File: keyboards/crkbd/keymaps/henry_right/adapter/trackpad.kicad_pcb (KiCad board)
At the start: 2 copper layers, 39.6 x 19.7 mm, 17 parts, among them J1 J1, U1 Elite-C-nf, U2 ProMicro, U3 U3, U4 NCP1117-2.85_SOT223

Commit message: 수정중
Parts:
- removed REF**: Hirose_FH12-12S-0.5SH_1x12-1MP_P0.50mm_Horizontal, Connector_FFC-FPC:Hirose_FH12-12S-0.5SH_1x12-1MP_P0.50mm_Horizontal
- removed REF**: SOIC-14_3.9x8.7mm_P1.27mm, Package_SO:SOIC-14_3.9x8.7mm_P1.27mm
- C1, C2: footprint Capacitor_Tantalum_SMD:CP_EIA-6032-15_Kemet-U -> Capacitor_SMD:C_0805_2012Metric
- C3: value 100pF -> 100nF
- J1: value J1 -> Conn_01x12; footprint trackpad:67997-410HLF -> Connector_FFC-FPC:Hirose_FH12-12S-0.5SH_1x12-1MP_P0.50mm_Horizontal
- U1: value Elite-C-nf -> Elite-C
- U3: value U3 -> NCP1117-3.3_SOT223; footprint trackpad:TXB0106PWR -> Package_TO_SOT_SMD:SOT-223-3_TabPin2
- U4: value NCP1117-2.85_SOT223 -> TXB0104D; footprint Package_TO_SOT_SMD:SOT-223-3_TabPin2 -> Package_SO:SOIC-14_3.9x8.7mm_P1.27mm
- moved J1 42.9 mm to (98.5, 63.0)
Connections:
- C2 pad 1: +2V8 -> +3V3
- C3 pad 1: +5V -> +3V3
- J1 pad 1: +2V8 -> +3V3
- J1 pad 10: GND -> TP_CS_3V3
- J1 pad 2: TP_SHUTDOWN_2V85 -> GND
- J1 pad 3: MOSI_2V85 -> Net-(J1-Pad3)
- J1 pad 4: SCK_2V85 -> Net-(J1-Pad4)
- J1 pad 5: GND -> Net-(J1-Pad5)
- J1 pad 6: TP_MOTION_2V85 -> Net-(J1-Pad6)
- J1 pad 7: TP_CS_2V85 -> Net-(J1-Pad7)
- J1 pad 8: MISO_2V85 -> MOSI_3V3
- J1 pad 9: Net-(J1-Pad9) -> PB6
- R1 pad 1: Net-(R1-Pad1) -> LVL_SHIFT
- U1 pad 1: TP_MOTION -> PD3
- U1 pad 25: PB7 -> LVL_SHIFT
- U1 pad 26: PD5 -> MAP_B0D5
- U1 pad 27: LVL_SHIFT -> MAP_B1C7
- U1 pad 28: TP_RESET -> MAP_B3F1
- U1 pad 29: TP_SHUTDOWN -> MAP_B2F0
- U2 pad 1: PB5 -> PD3
- U2 pad 12: Net-(U2-Pad12) -> PB5
- U2 pad 14: Net-(U2-Pad14) -> MAP_B2F0
- U2 pad 15: PD5 -> MAP_B3F1
- U2 pad 16: PB7 -> MAP_B1C7
- U2 pad 24: Net-(U2-Pad24) -> MAP_B0D5
- U3 pad 1: TP_MOTION_2V85 -> GND
- U3 pad 2: +2V8 -> +3V3
- U3 pad 3: TP_CS_2V85 -> +5V
- U4 pad 1: GND -> +3V3
- U4 pad 2: +2V8 -> TP_CS_3V3
- U4 pad 3: +5V -> MOSI_3V3
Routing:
- net TP_MOTION: track 28.5 -> 0.00 mm, vias 1 -> 0
- net PD3: track 0.00 -> 28.5 mm, vias 0 -> 1
- net +3V3: track 0.00 -> 21.2 mm
- net +2V8: track 48.1 -> 27.6 mm
- net TP_SHUTDOWN_2V85: track 11.0 -> 0.00 mm
- net +5V: track 24.3 -> 13.8 mm
- net MOSI_2V85: track 10.2 -> 0.00 mm
- net PB7: track 21.5 -> 16.1 mm
- net PD5: track 20.9 -> 17.4 mm
- net TP_RESET: track 4.20 -> 0.97 mm
- net PB5: track 34.8 -> 31.7 mm
- net TP_CS: track 32.9 -> 29.8 mm
- net TP_SHUTDOWN: track 15.3 -> 13.0 mm
- net LVL_SHIFT: track 2.09 -> 0.18 mm
- net TP_MOTION_2V85: track 15.7 -> 14.1 mm
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
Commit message: 배치 시작
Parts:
- removed C5: 100pF, Capacitor_SMD:C_0805_2012Metric
- removed C6: 100nF, Capacitor_SMD:C_0805_2012Metric
- removed R2, R4: 2.5K, Resistor_SMD:R_0805_2012Metric
- removed R3: 3.3K, Resistor_SMD:R_0805_2012Metric
- J1: moved to B.Cu
- moved C3 25.2 mm to (130.8, 66.0)
- moved J1 25.2 mm to (86.4, 85.1), turned to 90 degrees
- moved U4 22.7 mm to (84.9, 63.5)
- moved U3 22.0 mm to (104.8, 63.5)
- moved C4 21.7 mm to (124.5, 63.2)
- moved C1 21.1 mm to (119.0, 67.3)
- moved C2 14.6 mm to (115.9, 62.2)
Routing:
- net GND: track 61.5 -> 1.80 mm, vias 3 -> 0
- net PB5: track 31.7 -> 0.76 mm, vias 2 -> 0
- net TP_CS: track 29.8 -> 1.14 mm, vias 1 -> 0
- net PD3: track 28.5 -> 0.00 mm, vias 1 -> 0
- net +2V8: track 27.6 -> 0.00 mm
- net +3V3: track 21.2 -> 0.00 mm
- net PD5: track 17.4 -> 0.00 mm, vias 4 -> 0
- net PB7: track 16.1 -> 0.00 mm, vias 4 -> 0
- net SCK_2V85: track 14.9 -> 0.00 mm, vias 1 -> 0
- net TP_CS_2V85: track 14.9 -> 0.00 mm, vias 1 -> 0
- net MISO_2V85: track 14.7 -> 0.00 mm, vias 1 -> 0
- net TP_MOTION_2V85: track 14.1 -> 0.00 mm, vias 1 -> 0
- net TP_SHUTDOWN: track 13.0 -> 0.00 mm
- net MOSI: track 13.3 -> 0.80 mm
- net +5V: track 13.8 -> 2.82 mm
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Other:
- board text added: "GlidePoint Circle Adapter Henry Jian"
- board text removed: "Trackpad controller v1.1 Designed by vlukash"

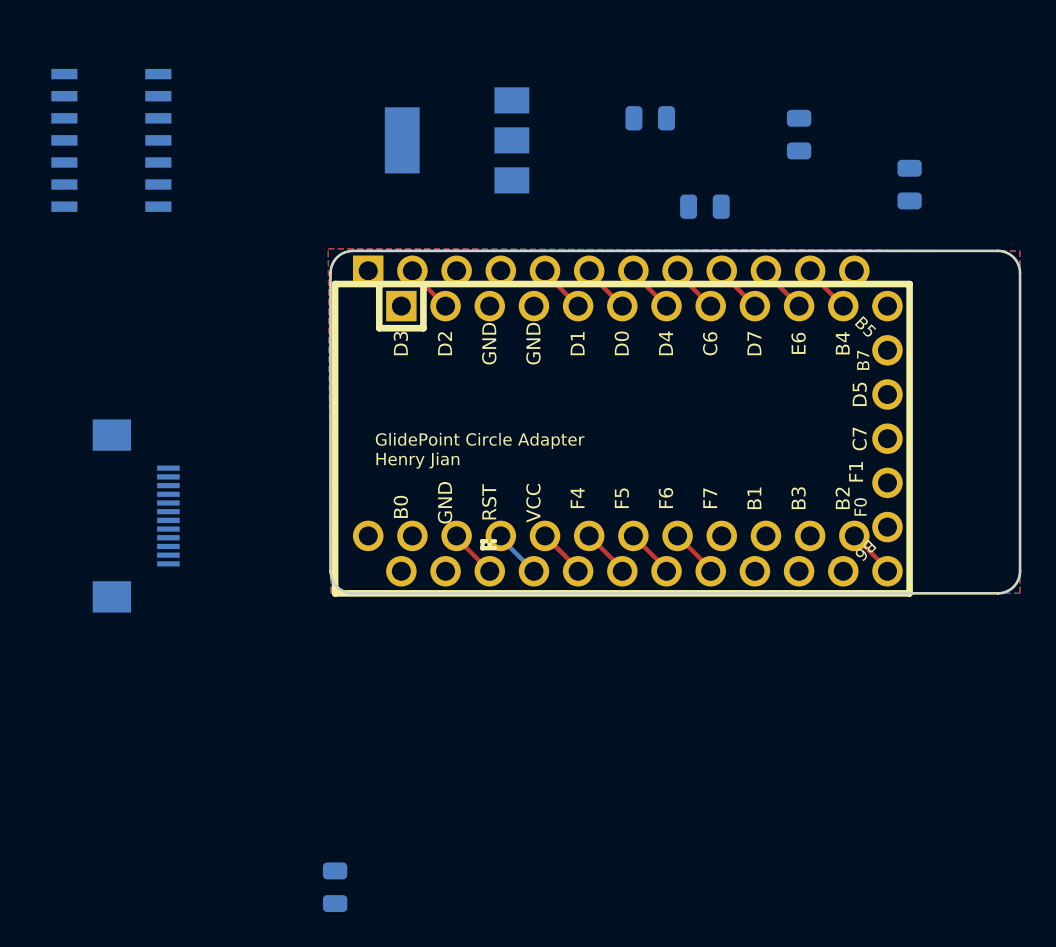
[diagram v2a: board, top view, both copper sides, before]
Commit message: 배치 거의 끝난듯
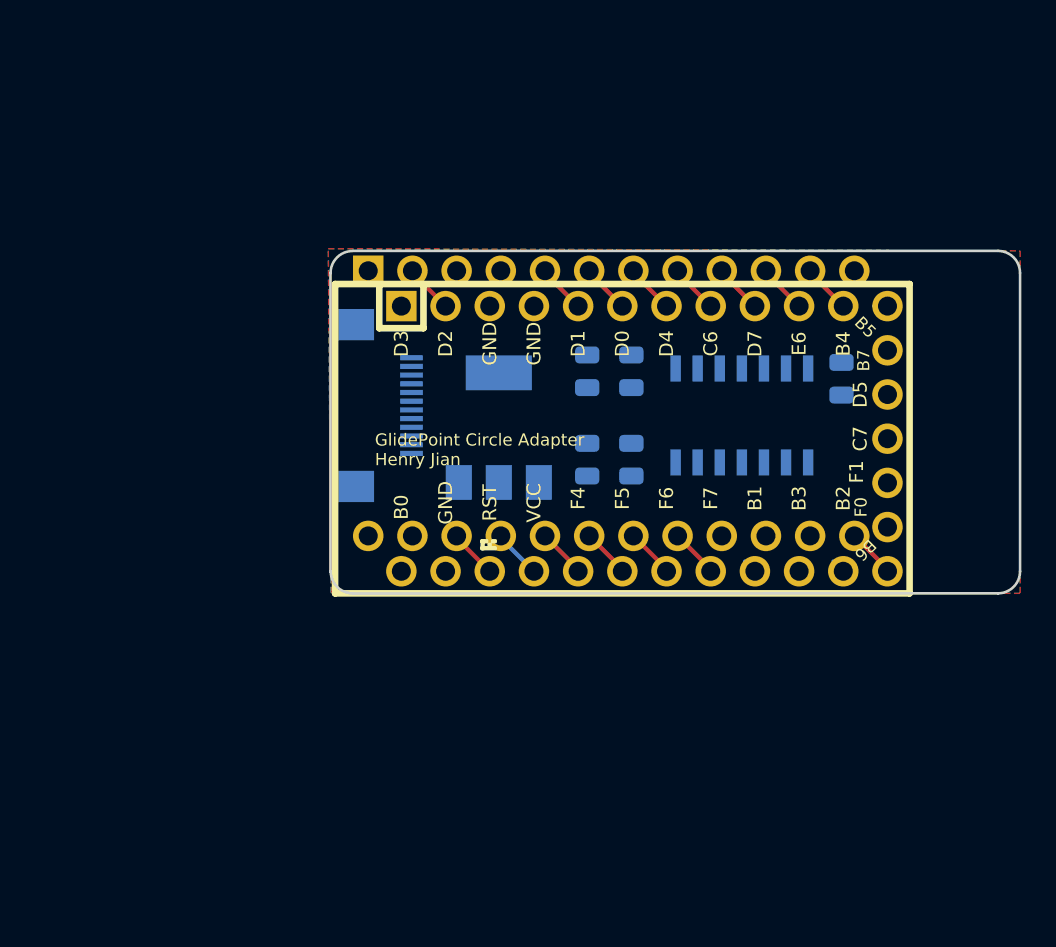
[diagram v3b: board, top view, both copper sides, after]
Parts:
- moved R1 41.2 mm to (126.9, 77.2), turned to 90 degrees
- moved U4 39.5 mm to (121.2, 79.3), turned to 270 degrees
- moved C4 21.0 mm to (114.8, 81.8), turned to 90 degrees
- moved C3 19.3 mm to (114.8, 76.8)
- moved U3 16.7 mm to (107.2, 80.0), turned to 90 degrees
- moved C1 16.0 mm to (112.3, 81.8), turned to 90 degrees
- moved J1 15.3 mm to (100.3, 78.7)
- moved C2 15.0 mm to (112.3, 76.8), turned to 270 degrees
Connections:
- U4 pad 10: SCK -> MOSI
- U4 pad 12: MOSI -> SCK
- U4 pad 3: MOSI_3V3 -> SCK_3V3
- U4 pad 5: SCK_3V3 -> MOSI_3V3

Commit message: drc통과
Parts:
- turned C2 to 90 degrees
- turned C3 to 90 degrees
- turned R1 to 270 degrees
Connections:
- J1 pad 9: PB6 -> PD2
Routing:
- net MAP_B0D5: track 0.00 -> 33.2 mm, vias 0 -> 1
- net MOSI_3V3: track 0.00 -> 22.7 mm
- net MISO_3V3: track 0.00 -> 21.4 mm, vias 0 -> 2
- net TP_CS: track 1.14 -> 21.8 mm, vias 0 -> 1
- net SCK_3V3: track 0.00 -> 19.0 mm
- net TP_CS_3V3: track 0.00 -> 18.9 mm
- net +3V3: track 0.00 -> 17.1 mm
- net +5V: track 2.82 -> 19.0 mm
- net GND: track 1.80 -> 13.9 mm, vias 0 -> 8
- net MAP_B1C7: track 0.00 -> 11.8 mm
- net LVL_SHIFT: track 0.00 -> 9.47 mm
- net MOSI: track 0.80 -> 9.33 mm
- net MAP_B3F1: track 0.00 -> 8.25 mm
- net MISO: track 0.00 -> 7.62 mm
- net PD2: track 3.38 -> 10.9 mm
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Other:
- board size 39.6 x 19.7 mm -> 33.6 x 19.7 mm

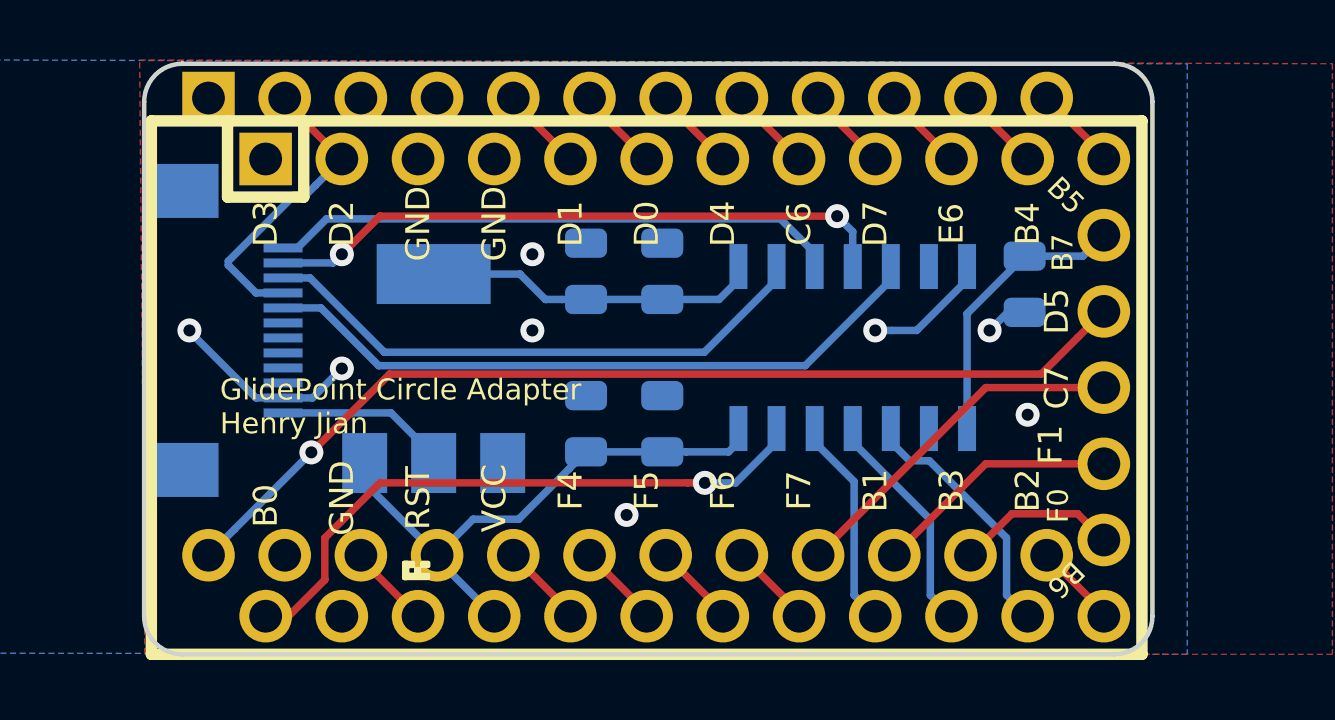
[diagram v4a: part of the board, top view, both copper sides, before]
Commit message: 실크스크린 처리
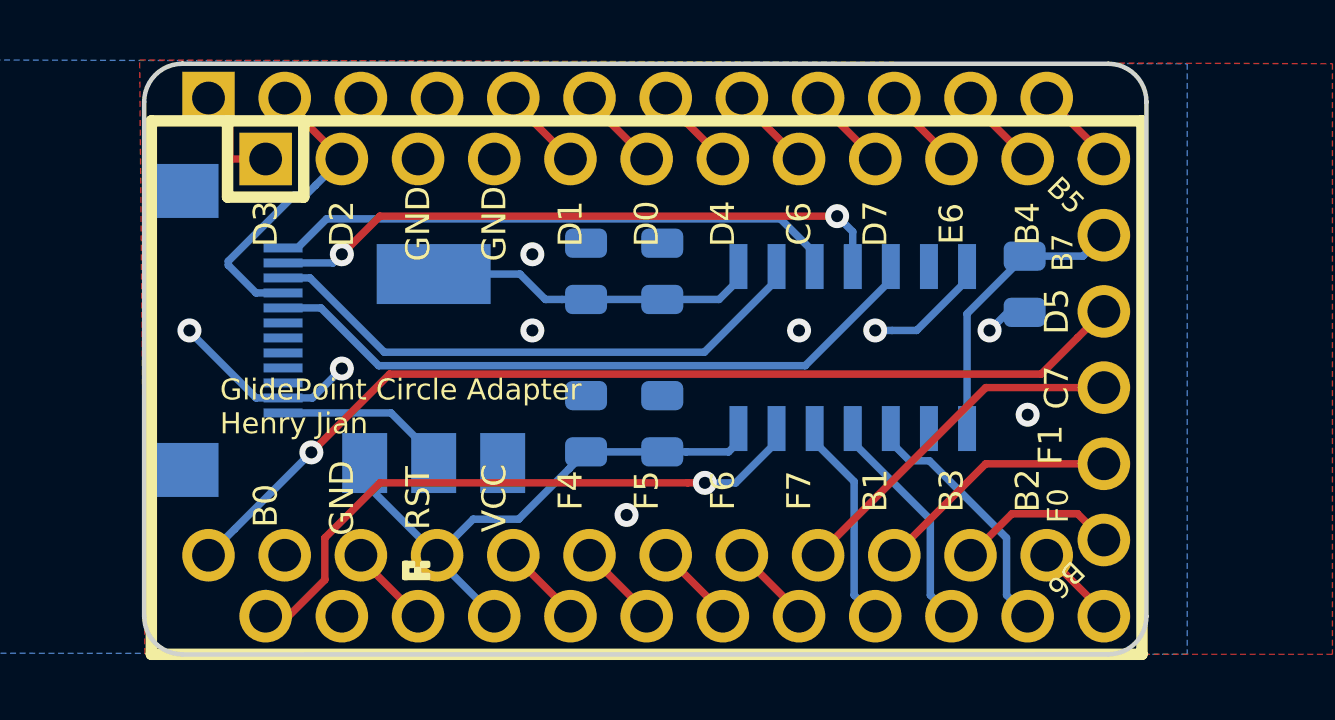
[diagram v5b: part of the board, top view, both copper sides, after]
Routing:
- net PD3: track 0.00 -> 2.47 mm
- net GND: vias 8 -> 9
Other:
- board size 33.6 x 19.7 mm -> 33.4 x 19.7 mm
- board text added: ".1u"
- board text added: "10u"
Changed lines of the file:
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@@
   (general
     (thickness 1.6)
-    (drawings 10)
-    (tracks 160)
+    (drawings 12)
+    (tracks 165)
     (zones 0)
     (modules 10)
@@
   )
   (layers
-    (0 F.Cu signal hide)
-    (31 B.Cu signal hide)
+    (0 F.Cu signal)
+    (31 B.Cu signal)
     (32 B.Adhes user hide)
     (33 F.Adhes user hide)
@@
     (35 F.Paste user hide)
     (36 B.SilkS user)
-    (37 F.SilkS user hide)
+    (37 F.SilkS user)
     (38 B.Mask user hide)
     (39 F.Mask user hide)
@@
     (tags capacitor)
     (attr smd)
-    (fp_text reference C3 (at 0 1.65 270) (layer B.SilkS)
+    (fp_text reference C3 (at 0 1.65 270) (layer B.SilkS) hide
       (effects (font (size 1 1) (thickness 0.15)) (justify mirror))
     )
@@
     (tags capacitor)
     (attr smd)
-    (fp_text reference C4 (at 0 1.65 90) (layer B.SilkS)
+    (fp_text reference C4 (at 0 1.65 90) (layer B.SilkS) hide
       (effects (font (size 1 1) (thickness 0.15)) (justify mirror))
     )
@@
     (tags resistor)
     (attr smd)
-    (fp_text reference R1 (at 0 1.65 270) (layer B.SilkS)
+    (fp_text reference R1 (at 2.81 -0.1 270) (layer B.SilkS)
       (effects (font (size 1 1) (thickness 0.15)) (justify mirror))
     )
@@
     (tags capacitor)
     (attr smd)
-    (fp_text reference C1 (at 0 1.65 90) (layer B.SilkS)
+    (fp_text reference C1 (at 0 1.65 90) (layer B.SilkS) hide
       (effects (font (size 1 1) (thickness 0.15)) (justify mirror))
     )
@@
     (tags capacitor)
     (attr smd)
-    (fp_text reference C2 (at 0 1.65 270) (layer B.SilkS)
+    (fp_text reference C2 (at 0 1.65 270) (layer B.SilkS) hide
       (effects (font (size 1 1) (thickness 0.15)) (justify mirror))
     )
@@
     (tags "connector Hirose FH12 horizontal")
     (attr smd)
-    (fp_text reference J1 (at 0 3.7 90) (layer B.SilkS)
+    (fp_text reference J1 (at 0 0 90) (layer B.SilkS)
       (effects (font (size 1 1) (thickness 0.15)) (justify mirror))
     )
@@
     (tags "CMS SOT")
     (attr smd)
-    (fp_text reference U3 (at 0 4.5 90) (layer B.SilkS)
+    (fp_text reference U3 (at 0 0.75 90) (layer B.SilkS)
       (effects (font (size 1 1) (thickness 0.15)) (justify mirror))
     )
@@
     (tags "SOIC 1.27")
     (attr smd)
-    (fp_text reference U4 (at 0 5.375 270) (layer B.SilkS)
+    (fp_text reference U4 (at 0 3.06 270) (layer B.SilkS)
       (effects (font (size 1 1) (thickness 0.15)) (justify mirror))
     )
@@
     )
   )
+  (gr_text .1u (at 114.8 79.34 90) (layer B.SilkS)
+    (effects (font (size 0.7 0.7) (thickness 0.15)) (justify mirror))
+  )
+  (gr_text 10u (at 112.26 79.34 90) (layer B.SilkS)
+    (effects (font (size 0.7 0.7) (thickness 0.15)) (justify mirror))
+  )
   (gr_line (start 98.82 69.85) (end 98.83 69.85) (layer Edge.Cuts) (width 0.15))
   (gr_text "GlidePoint Circle Adapter\nHenry Jian" (at 100.076 81.28) (layer F.SilkS)
     (effects (font (size 0.7 0.7) (thickness 0.175)) (justify left))
   )
-  (gr_arc (start 129.89 71.12) (end 131.16 71.12) (angle -90) (layer Edge.Cuts) (width 0.15))
-  (gr_arc (start 129.89 88.265) (end 129.89 89.535) (angle -90) (layer Edge.Cuts) (width 0.15))
+  (gr_arc (start 129.69 71.12) (end 130.96 71.12) (angle -90) (layer Edge.Cuts) (width 0.15))
+  (gr_arc (start 129.69 88.265) (end 129.69 89.535) (angle -90) (layer Edge.Cuts) (width 0.15))
   (gr_arc (start 98.82 88.265) (end 97.55 88.265) (angle -90) (layer Edge.Cuts) (width 0.15))
   (gr_arc (start 98.82 71.12) (end 98.82 69.85) (angle -90) (layer Edge.Cuts) (width 0.15))
   (gr_line (start 97.55 88.265) (end 97.55 71.12) (layer Edge.Cuts) (width 0.15))
-  (gr_line (start 129.89 89.535) (end 98.82 89.54) (layer Edge.Cuts) (width 0.15))
-  (gr_line (start 131.16 71.12) (end 131.16 88.265) (layer Edge.Cuts) (width 0.15))
-  (gr_line (start 98.83 69.85) (end 129.89 69.85) (layer Edge.Cuts) (width 0.15))
+  (gr_line (start 129.69 89.535) (end 98.82 89.54) (layer Edge.Cuts) (width 0.15))
+  (gr_line (start 130.96 71.12) (end 130.96 88.265) (layer Edge.Cuts) (width 0.15))
+  (gr_line (start 98.83 69.85) (end 129.69 69.85) (layer Edge.Cuts) (width 0.15))
+  (via (at 119.38 78.74) (size 0.8) (drill 0.4) (layers F.Cu B.Cu) (net 1))
   (via (at 113.63 84.89) (size 0.8) (drill 0.4) (layers F.Cu B.Cu) (net 1))
   (via (at 110.49 78.74) (size 0.8) (drill 0.4) (layers F.Cu B.Cu) (net 1))
@@
   (segment (start 105.78 81.49) (end 107.2 82.91) (width 0.25) (layer B.Cu) (net 23))
   (segment (start 102.18 81.49) (end 105.78 81.49) (width 0.25) (layer B.Cu) (net 23))
+  (segment (start 100.403398 71.738179) (end 100.405559 71.712549) (width 0.25) (layer F.Cu) (net 29))
+  (segment (start 100.4737 73.025) (end 100.403398 72.954698) (width 0.25) (layer F.Cu) (net 29))
+  (segment (start 100.403398 72.954698) (end 100.403398 71.738179) (width 0.25) (layer F.Cu) (net 29))
+  (segment (start 101.6 73.025) (end 100.4737 73.025) (width 0.25) (layer F.Cu) (net 29))
   (segment (start 128.663701 84.848701) (end 129.54 85.725) (width 0.25) (layer F.Cu) (net 30))
   (segment (start 126.479299 84.848701) (end 128.663701 84.848701) (width 0.25) (layer F.Cu) (net 30))
